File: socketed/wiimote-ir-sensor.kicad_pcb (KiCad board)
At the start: 2 copper layers, 13.5 x 16.2 mm, 11 parts, among them J1 Conn_01x04_Pin, U2 AP2112-3.3V, X1 SG3225CAN 24.0000M-TJGA3

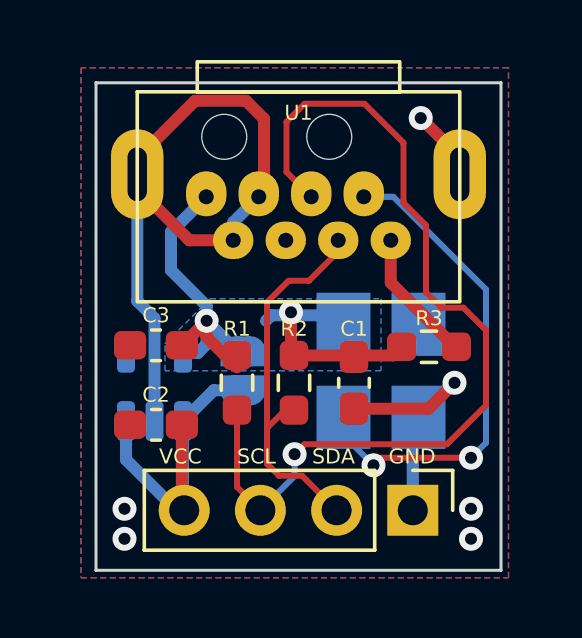
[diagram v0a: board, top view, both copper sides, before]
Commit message: Cheaper PCBA (#3)
* Move all components to one side of the board for cheaper PCBA

* Socketed: Add option to wire CLK directly
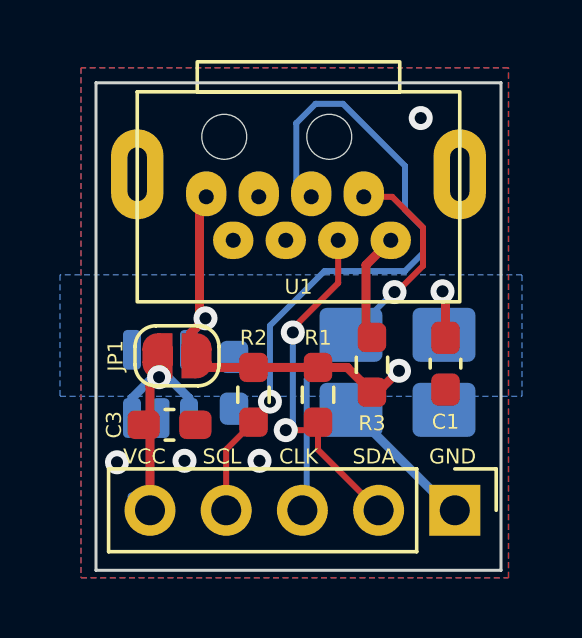
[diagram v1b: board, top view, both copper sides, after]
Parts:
- C2: moved to B.Cu
- J1: value Conn_01x04_Pin -> Conn_01x05_Pin; footprint Connector_PinHeader_2.54mm:PinHeader_1x04_P2.54mm_Vertical -> Connector_PinHeader_2.54mm:PinHeader_1x05_P2.54mm_Vertical
- JP1: moved to F.Cu
- U1: footprint GUN4IR:wiimote-pixart-camera -> wiimote-ir-sensor:wiimote-pixart-camera
- moved C1 3.12 mm to (161.7, 109.4)
- moved C2 2.95 mm to (154.6, 110.0), turned to -90 degrees
- moved R1 2.73 mm to (157.4, 110.4)
- moved C3 2.69 mm to (152.4, 111.4), turned to 0 degrees
- moved JP1 2.26 mm to (152.7, 109.1), turned to 0 degrees
- moved R3 1.99 mm to (159.2, 109.4), turned to 90 degrees
- moved R2 1.41 mm to (155.2, 110.4)
- moved J1 1.40 mm to (162.0, 114.2)
- moved X1 0.55 mm to (160.1, 109.7), turned to 180 degrees
- moved U2 0.22 mm to (152.2, 110.0)
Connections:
- C2 pad 1: +5V -> +3.3V
- C3 pad 1: +3.3V -> VCC
- J1 pad 3: /SCL -> /CLK
- J1 pad 4: +5V -> /SCL
- JP1 pad 1: +5V -> VCC
- R1 pad 2: /SCL -> /SDA
- R2 pad 1: /SDA -> /SCL
- U2 pad 1: +5V -> VCC
- U2 pad 3: +5V -> VCC
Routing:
- net GND: track 31.9 -> 4.72 mm, vias 6 -> 4
- net +5V: track 12.6 -> 0.00 mm
- net VCC: track 0.00 -> 9.00 mm, vias 0 -> 1
- net /SCL: track 30.9 -> 23.4 mm
- net +3.3V: track 19.1 -> 16.3 mm, vias 2 -> 3
- net /CLK: track 16.5 -> 13.9 mm, vias 2 -> 1
- net /SDA: track 13.1 -> 12.0 mm, vias 0 -> 2
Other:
- board text added: "CLK"
